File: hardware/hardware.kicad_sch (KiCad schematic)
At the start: 214 parts, among them J1 USB_B_Micro, J2 RJ45_Hanrun_HR911105A_Horizon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, J3 Conn_02x05_Odd_Even, J4 Conn_02x03_Odd_Even, J5 Conn_01x02, U10 CH32V003F4P6, U11 CH32V003F4P6, U12 CH32V003F4P6, U13 CH32V003F4P6, U14 CH32V003F4P6, U15 CH32V003F4P6, U16 CH32V003F4P6, U17 CH32V003F4P6, U18 CH32V003F4P6, U19 CH32V003F4P6, U2 CH32V003F4P6, U20 CH32V003F4P6, U21 CH32V003F4P6, U22 CH32V003F4P6, U23 CH32V003F4P6, U24 CH32V003F4P6, U25 CH32V003F4P6, U26 CH32V003F4P6, U27 CH32V003F4P6, U28 CH32V307RCT6, U3 AMS1117-3.3, U4 CH340C, U5 CH32V003F4P6, U6 CH32V003F4P6, U7 CH32V003F4P6, U8 CH32V003F4P6, U9 CH32V003F4P6, Y1 Crystal_GND24

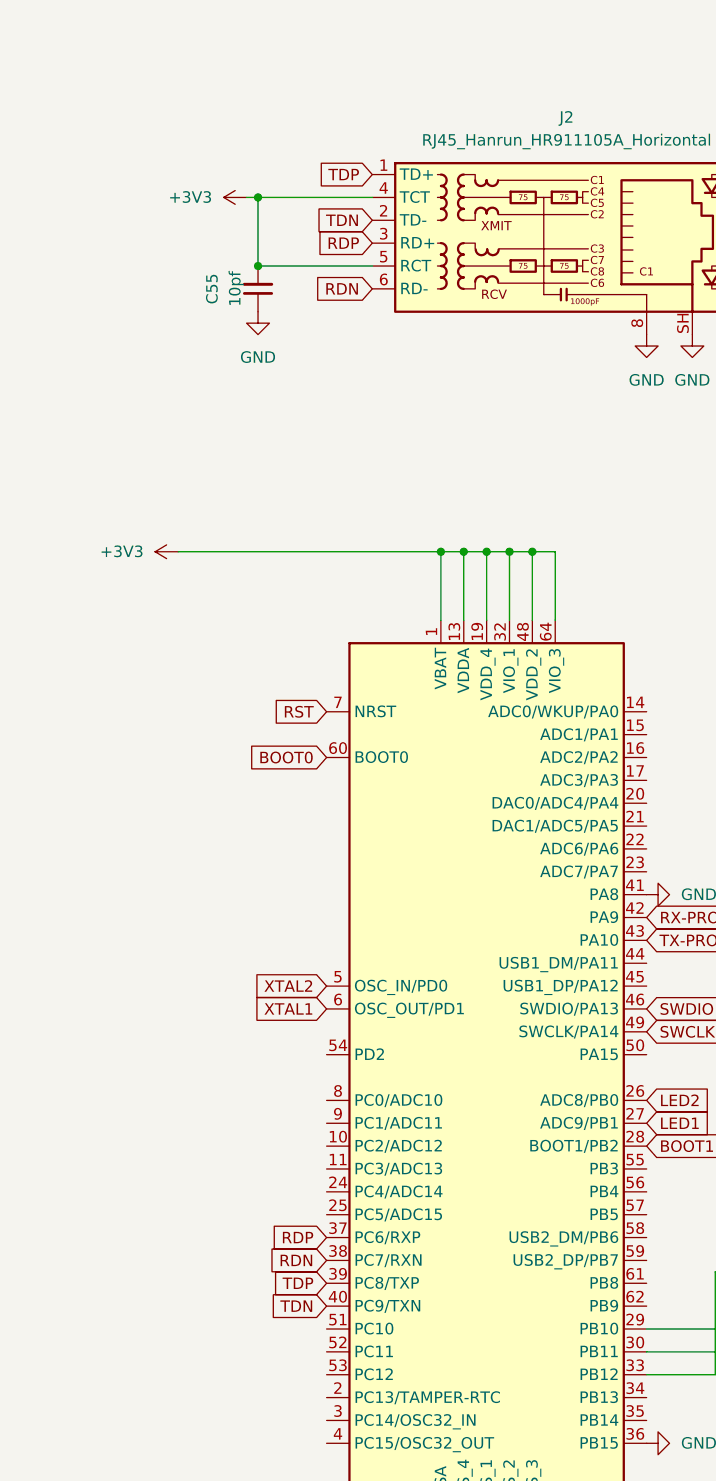
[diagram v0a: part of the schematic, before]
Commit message: pass to 4 layers pcb
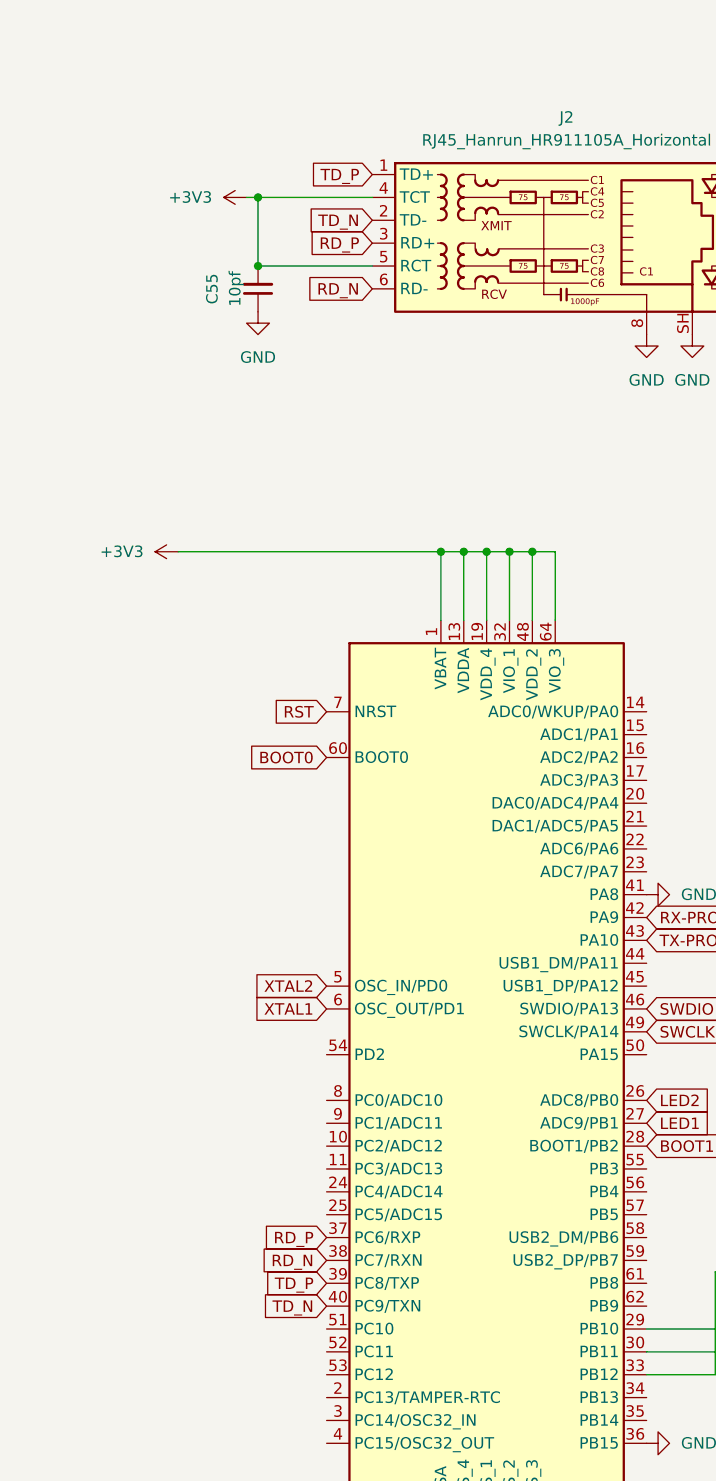
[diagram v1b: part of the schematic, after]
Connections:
- net RDN renamed RD_N
- net RDP renamed RD_P
- net TDN renamed TD_N
- net TDP renamed TD_P
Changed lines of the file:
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@@
 		)
 	)
-	(global_label "RDP"
+	(global_label "RD_P"
 		(shape input)
 		(at 54.61 139.7 180)
@@
 		)
 		(property "Intersheetrefs" "${INTERSHEET_REFS}"
-			(at 47.8148 139.7 0)
+			(at 46.8472 139.7 0)
 			(effects
 				(font
@@
 		)
 	)
-	(global_label "TDP"
+	(global_label "TD_P"
 		(shape input)
 		(at 49.53 255.27 180)
@@
 		)
 		(property "Intersheetrefs" "${INTERSHEET_REFS}"
-			(at 43.0372 255.27 0)
-			(effects
-				(font
-					(size 1.27 1.27)
-				)
-				(justify right)
-				(hide yes)
-			)
-		)
-	)
-	(global_label "RDP"
+			(at 42.0696 255.27 0)
+			(effects
+				(font
+					(size 1.27 1.27)
+				)
+				(justify right)
+				(hide yes)
+			)
+		)
+	)
+	(global_label "RD_P"
 		(shape input)
 		(at 49.53 250.19 180)
@@
 		)
 		(property "Intersheetrefs" "${INTERSHEET_REFS}"
-			(at 42.7348 250.19 0)
+			(at 41.7672 250.19 0)
 			(effects
 				(font
@@
 		)
 	)
-	(global_label "RDN"
+	(global_label "RD_N"
 		(shape input)
 		(at 49.53 252.73 180)
@@
 		)
 		(property "Intersheetrefs" "${INTERSHEET_REFS}"
-			(at 42.6743 252.73 0)
+			(at 41.7067 252.73 0)
 			(effects
 				(font
@@
 		)
 	)
-	(global_label "TDN"
+	(global_label "TD_N"
 		(shape input)
 		(at 54.61 137.16 180)
@@
 		)
 		(property "Intersheetrefs" "${INTERSHEET_REFS}"
-			(at 48.0567 137.16 0)
+			(at 47.0891 137.16 0)
 			(effects
 				(font
@@
 		)
 	)
-	(global_label "RDN"
+	(global_label "RD_N"
 		(shape input)
 		(at 54.61 144.78 180)
@@
 		)
 		(property "Intersheetrefs" "${INTERSHEET_REFS}"
-			(at 47.7543 144.78 0)
+			(at 46.7867 144.78 0)
 			(effects
 				(font
@@
 		)
 	)
-	(global_label "TDP"
+	(global_label "TD_P"
 		(shape input)
 		(at 54.61 132.08 180)
@@
 		)
 		(property "Intersheetrefs" "${INTERSHEET_REFS}"
-			(at 48.1172 132.08 0)
+			(at 47.1496 132.08 0)
 			(effects
 				(font
@@
 		)
 	)
-	(global_label "TDN"
+	(global_label "TD_N"
 		(shape input)
 		(at 49.53 257.81 180)
@@
 		)
 		(property "Intersheetrefs" "${INTERSHEET_REFS}"
-			(at 42.9767 257.81 0)
-			(effects
-				(font
+			(at 42.0091 257.81 0)
+			(effects
+				(font
